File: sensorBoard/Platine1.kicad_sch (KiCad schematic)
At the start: 14 parts, among them J10 Conn_01x07, J11 Conn_01x03, J12 Conn_01x02, J13 Conn_01x04, J14 Conn_01x05, J15 Conn_01x02, J9 Conn_01x04, U17 LD1117S33TR_SOT223

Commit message: Das erstes PCB ist fast fertig. Die Vias waren auf die Platine platziert und Poligon war gefüllt.
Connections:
- net microcontroller1/UART_RX: now also J10.2 (Pin_2); no longer J10.1 (Pin_1)
- net microcontroller1/UART_TX: now also J10.1 (Pin_1); no longer J10.2 (Pin_2)
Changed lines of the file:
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@@
 	(wire
 		(pts
+			(xy 34.29 116.84) (xy 50.8 116.84)
+		)
+		(stroke
+			(width 0)
+			(type default)
+		)
+	)
+	(wire
+		(pts
 			(xy 243.84 137.16) (xy 243.84 140.97)
 		)
@@
 	(wire
 		(pts
-			(xy 50.8 114.3) (xy 36.83 114.3)
-		)
-		(stroke
-			(width 0)
-			(type default)
-		)
-	)
-	(wire
-		(pts
 			(xy 39.37 124.46) (xy 50.8 124.46)
 		)
@@
 	(wire
 		(pts
-			(xy 34.29 116.84) (xy 50.8 116.84)
-		)
-		(stroke
-			(width 0)
-			(type default)
-		)
-	)
-	(wire
-		(pts
 			(xy 250.19 120.65) (xy 250.19 123.19)
 		)
@@
 	(wire
 		(pts
+			(xy 36.83 114.3) (xy 50.8 114.3)
+		)
+		(stroke
+			(width 0)
+			(type default)
+		)
+	)
+	(wire
+		(pts
 			(xy 232.41 146.05) (xy 232.41 143.51)
 		)
@@
 		)
 		(pin "UART_RX" input
-			(at 50.8 116.84 180)
+			(at 50.8 114.3 180)
 			(effects
 				(font
@@
 		)
 		(pin "UART_TX" output
-			(at 50.8 114.3 180)
+			(at 50.8 116.84 180)
 			(effects
 				(font

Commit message: aktualisierte Platine mit verschiedenen Stecker
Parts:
- removed J11: Conn_01x03, heder box:662103145021, symbol Connector_Generic:Conn_01x03
- removed J14: Conn_01x05, heder box:662105145021, symbol Connector_Generic:Conn_01x05
- removed J15: Conn_01x02, Connector_Phoenix_MC_HighVoltage:PhoenixContact_MCV_1,5_2-G-5.08_1x02_P5.08mm_Vertical, symbol Connector_Generic:Conn_01x02
- added J1, J2, J3: Conn_01x04, 6432101004xx:643210100404, symbol Connector_Generic:Conn_01x04
- J13: footprint Connector_Phoenix_MC_HighVoltage:PhoenixContact_MCV_1,5_4-G-5.08_1x04_P5.08mm_Vertical -> 6432101004xx:643210100404
- J9: footprint Connector_Phoenix_MC_HighVoltage:PhoenixContact_MCV_1,5_4-G-5.08_1x04_P5.08mm_Vertical -> heder box:662104145021
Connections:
- net +3.3V: now also J1.1 (Pin_1)
- net Commutation1-1/POLE+: now also J3.1 (Pin_1), J3.4 (Pin_4)
- net Commutation1-1/POLE-: now also J3.2 (Pin_2), J3.3 (Pin_3)
- net Commutation1-1/SERVO_OUT: now also J2.2 (Pin_2)
- net GND: now also J1.2 (Pin_2), J2.3 (Pin_3)
- net I2C_SCL: now also J1.3 (Pin_3)
- net I2C_SDA: now also J1.4 (Pin_4)
- net Protection1/12V_IN: now also J9.1 (Pin_1); no longer J9.4 (Pin_4)
- net Protection1/5V_IN: now also J9.4 (Pin_4); no longer J9.1 (Pin_1)
- net SERVO_PWM: now also J2.1 (Pin_1)
- no-connect marks 0 -> 1

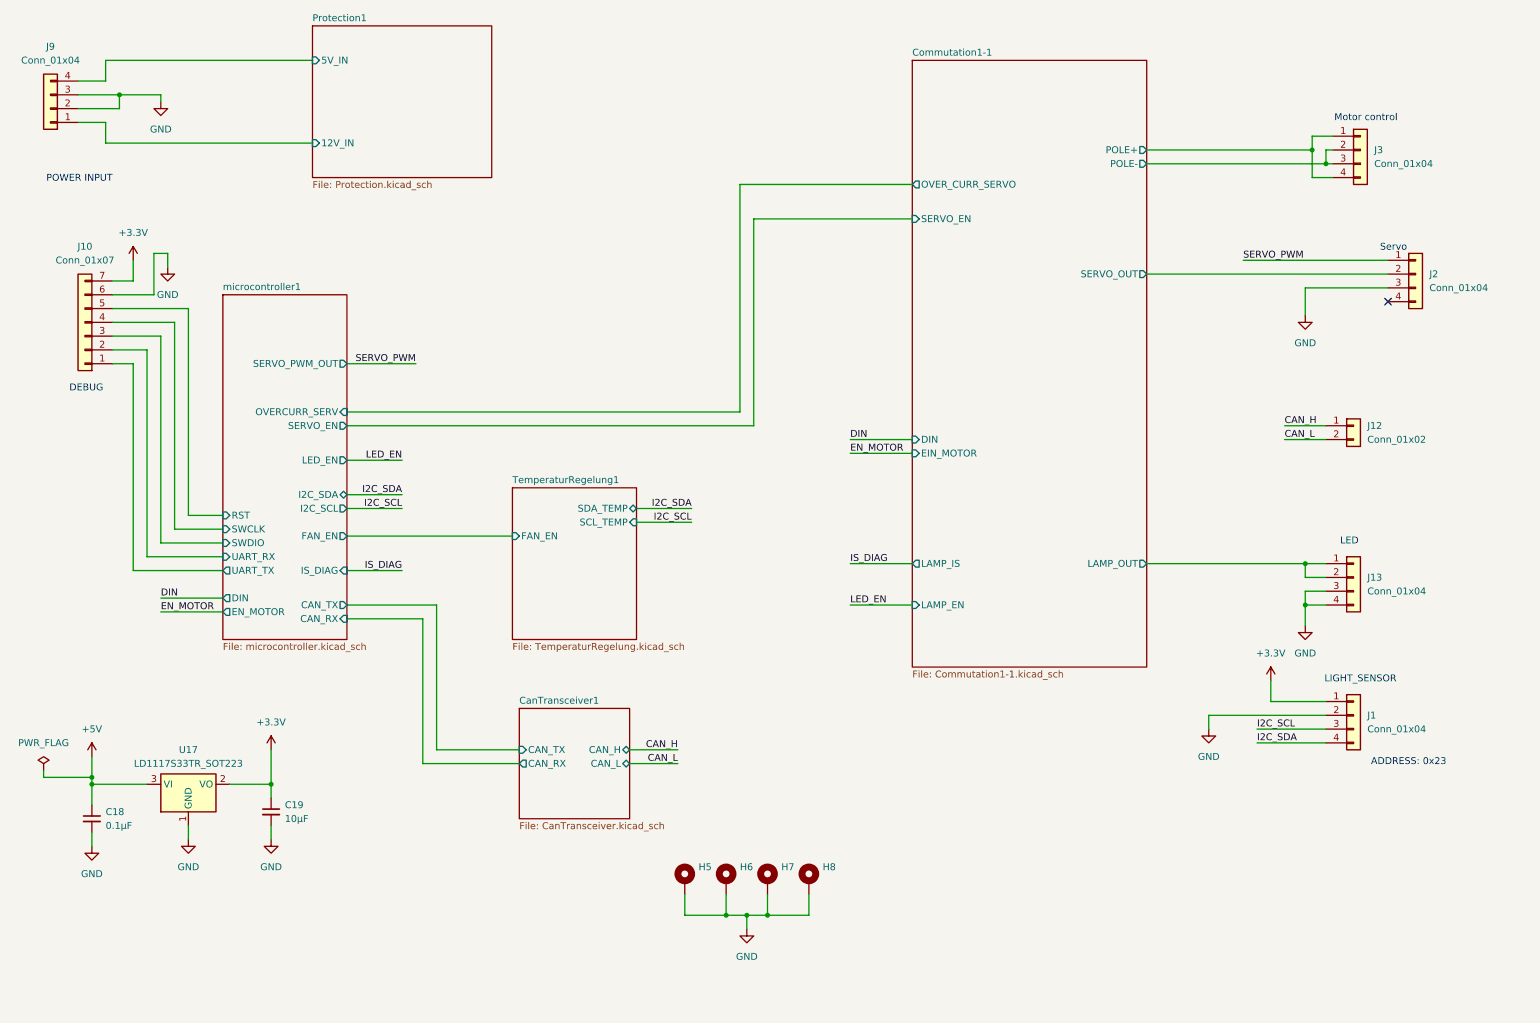
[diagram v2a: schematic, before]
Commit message: added old software + new PCB
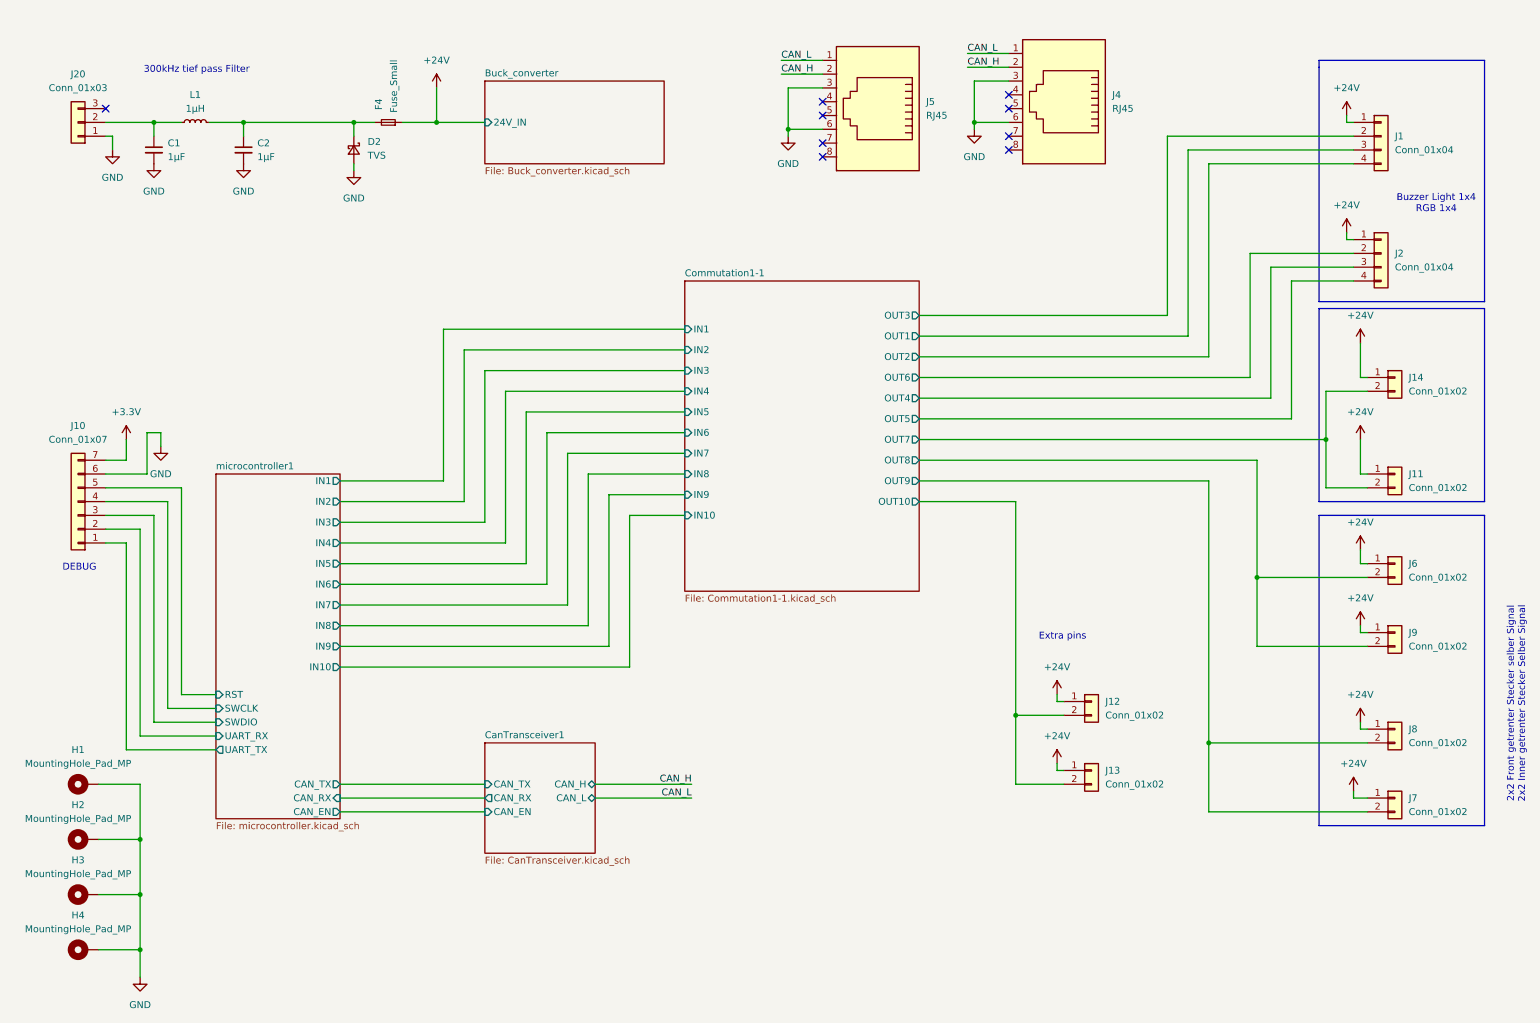
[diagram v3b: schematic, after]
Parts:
- removed C18: 0.1µF, Capacitor_SMD:C_0805_2012Metric, symbol Device:C_Small
- removed C19: 10µF, Capacitor_SMD:C_0805_2012Metric, symbol Device:C_Small
- removed H5, H6, H7, H8: MountingHole_Pad, MountingHole:MountingHole_4.3mm_M4_Pad_Via, symbol Mechanical:MountingHole_Pad
- removed J13, J3: Conn_01x04, 6432101004xx:643210100404, symbol Connector_Generic:Conn_01x04
- removed J9: Conn_01x04, heder box:662104145021, symbol Connector_Generic:Conn_01x04
- removed U17: LD1117S33TR_SOT223, Package_TO_SOT_SMD:SOT-223-3_TabPin2, symbol Regulator_Linear:LD1117S33TR_SOT223
- added C1, C2: 1µF, Capacitor_SMD:C_0603_1608Metric, symbol Device:C_Small
- added D2: TVS, Diode_SMD:D_SOD-323, symbol Device:D_Schottky_Small
- added F4: Fuse_Small, Fuse:Fuse_1206_3216Metric, symbol Device:Fuse_Small
- added H1, H2, H3, H4: MountingHole_Pad_MP, MountingHole:MountingHole_2.5mm_Pad_Via, symbol Mechanical:MountingHole_Pad_MP
- added J11, J14: Conn_01x02, Pavel_library:J_Wurth_WR-MPC3_662002231722, symbol Connector_Generic:Conn_01x02
- added J13, J6, J7, J8, J9: Conn_01x02, Pavel_library:J_Wurth_WR-MPC3_662102145021, symbol Connector_Generic:Conn_01x02
- added J20: Conn_01x03, Pavel_library:Untitled, symbol Connector_Generic:Conn_01x03
- added J4, J5: RJ45, Connector_RJ:RJ45_Amphenol_RJHSE5380, symbol Connector:RJ45
- added L1: 1µH, Inductor_SMD:L_Wuerth_WE-PD-Typ-7345, symbol Device:L_Small
- J1, J2: footprint 6432101004xx:643210100404 -> Pavel_library:J_Wurth_WR-MPC3_662004231722
- J12: footprint heder box:662102145021 -> Pavel_library:J_Wurth_WR-MPC3_662102145021
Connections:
- net +3.3V: no longer J1.1 (Pin_1)
- net CAN_H: now also J4.2, J5.2; no longer J12.1 (Pin_1)
- net CAN_L: now also J4.1, J5.1; no longer J12.2 (Pin_2)
- net GND: now also C1.2, C2.2, D2.2 (A), H1.MP, H2.MP, H3.MP, H4.MP, J20.1 (Pin_1), J4.3, J4.6, J5.3, J5.6; no longer J1.2 (Pin_2), J2.3 (Pin_3)
- net Commutation1-1/OUT5: now reaches J2.4 (Pin_4)
- net Commutation1-1/SERVO_OUT renamed Commutation1-1/OUT6
- net I2C_SCL renamed Commutation1-1/OUT1
- net I2C_SDA renamed Commutation1-1/OUT2
- net SERVO_PWM renamed +24V
- net +24V: now also J1.1 (Pin_1), J12.1 (Pin_1), F4.1, J11.1 (Pin_1), J13.1 (Pin_1), J14.1 (Pin_1), J6.1 (Pin_1), J7.1 (Pin_1), J8.1 (Pin_1), J9.1 (Pin_1)
- new net: C2.1, D2.1 (K), F4.2, L1.2
- new net: C1.1, J20.2 (Pin_2), L1.1
- new net Commutation1-1/OUT10: J12.2 (Pin_2), J13.2 (Pin_2)
- new net Commutation1-1/OUT3: J1.2 (Pin_2)
- new net Commutation1-1/OUT4: J2.3 (Pin_3)
- new net Commutation1-1/OUT7: J11.2 (Pin_2), J14.2 (Pin_2)
- new net Commutation1-1/OUT8: J6.2 (Pin_2), J9.2 (Pin_2)
- new net Commutation1-1/OUT9: J7.2 (Pin_2), J8.2 (Pin_2)
- no-connect marks 1 -> 9
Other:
- removed sheet Protection1
- removed sheet TemperaturRegelung1
- added sheet Buck_converter (Buck_converter.kicad_sch)
- sheet CanTransceiver1 ports: added CAN_EN; removed none
- sheet Commutation1-1 ports: added IN1, IN10, IN2, IN3, IN4, IN5, IN6, IN7, IN8, IN9, OUT1, OUT10, OUT2, OUT3, OUT4, OUT5, OUT6, OUT7, OUT8, OUT9; removed DIN, EIN_MOTOR, LAMP_EN, LAMP_IS, LAMP_OUT, OVER_CURR_SERVO, POLE+, POLE-, SERVO_EN, SERVO_OUT
- sheet microcontroller1 ports: added CAN_EN, IN1, IN10, IN2, IN3, IN4, IN5, IN6, IN7, IN8, IN9; removed DIN, EN_MOTOR, FAN_EN, I2C_SCL, I2C_SDA, IS_DIAG, LED_EN, OVERCURR_SERV, SERVO_EN, SERVO_PWM_OUT
- note added: "2x2 Front getrenter Stecker selber Signal 2x2 Inner getrenter Stecker Selber Signal"
- note added: "300kHz tief pass Filter"
- note added: "Buzzer Light 1x4 RGB 1x4"
- note added: "Extra pins"
- note removed: "ADDRESS: 0x23"
- note removed: "LED"
- note removed: "LIGHT_SENSOR"
- note removed: "Motor control"
- note removed: "POWER INPUT"
- note removed: "Servo"
- moved on the sheet: J10
